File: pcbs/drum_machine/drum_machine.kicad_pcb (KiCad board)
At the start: 2 copper layers, 171 x 97 mm, 128 parts, among them Q1 NPN, Q10 NPN, Q11 NPN, Q12 NPN, Q13 NPN, Q14 NPN, Q15 NPN, Q16 NPN, Q2 NPN, Q3 NPN, Q4 NPN, Q5 NPN, Q6 NPN, Q7 NPN, Q8 NPN, Q9 NPN, SW1 SW_SPDT, SW10 SW_SPDT, SW11 SW_SPDT, SW12 SW_SPDT, SW13 SW_SPDT, SW14 SW_SPDT, SW15 SW_SPDT, SW16 SW_SPDT, SW17 SW_SPDT, SW18 SW_SPDT, SW19 SW_SPDT, SW2 SW_SPDT, SW20 SW_SPDT, SW21 SW_SPDT, SW22 SW_SPDT, SW23 SW_SPDT, SW24 SW_SPDT, SW25 SW_SPDT, SW26 SW_SPDT, SW27 SW_SPDT, SW28 SW_SPDT, SW29 SW_SPDT, SW3 SW_SPDT, SW30 SW_SPDT, SW31 SW_SPDT, SW32 SW_SPDT, SW33 SW_SPDT, SW34 SW_SPDT, SW35 SW_SPDT, SW36 SW_SPDT, SW37 SW_SPDT, SW38 SW_SPDT, SW39 SW_SPDT, SW4 SW_SPDT, SW40 SW_SPDT, SW41 SW_SPDT, SW42 SW_SPDT, SW43 SW_SPDT, SW44 SW_SPDT, SW45 SW_SPDT, SW46 SW_SPDT, SW47 SW_SPDT, SW48 SW_SPDT, SW49 SW_SPDT_CYMBAL, SW5 SW_SPDT, SW50 SW_SPDT_COUNTOFF, SW51 SW_SPDT_PLAYSTOP, SW52 SW_SPDT_LEDS, SW53 SW_SPDT_TIMESIG, SW54 SW_SPDT_RESERVED0, SW55 SW_SPDT_RESERVED1, SW56 SW_SPDT_RESERVED2, SW6 SW_SPDT, SW7 SW_SPDT, SW8 SW_SPDT, SW9 SW_SPDT, U1 CD4051B, U10 CD4051B, U11 CD4051B, U12 CD4051B, U2 Pico, U3 CD4051B, U4 CD4051B, U5 CD4051B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

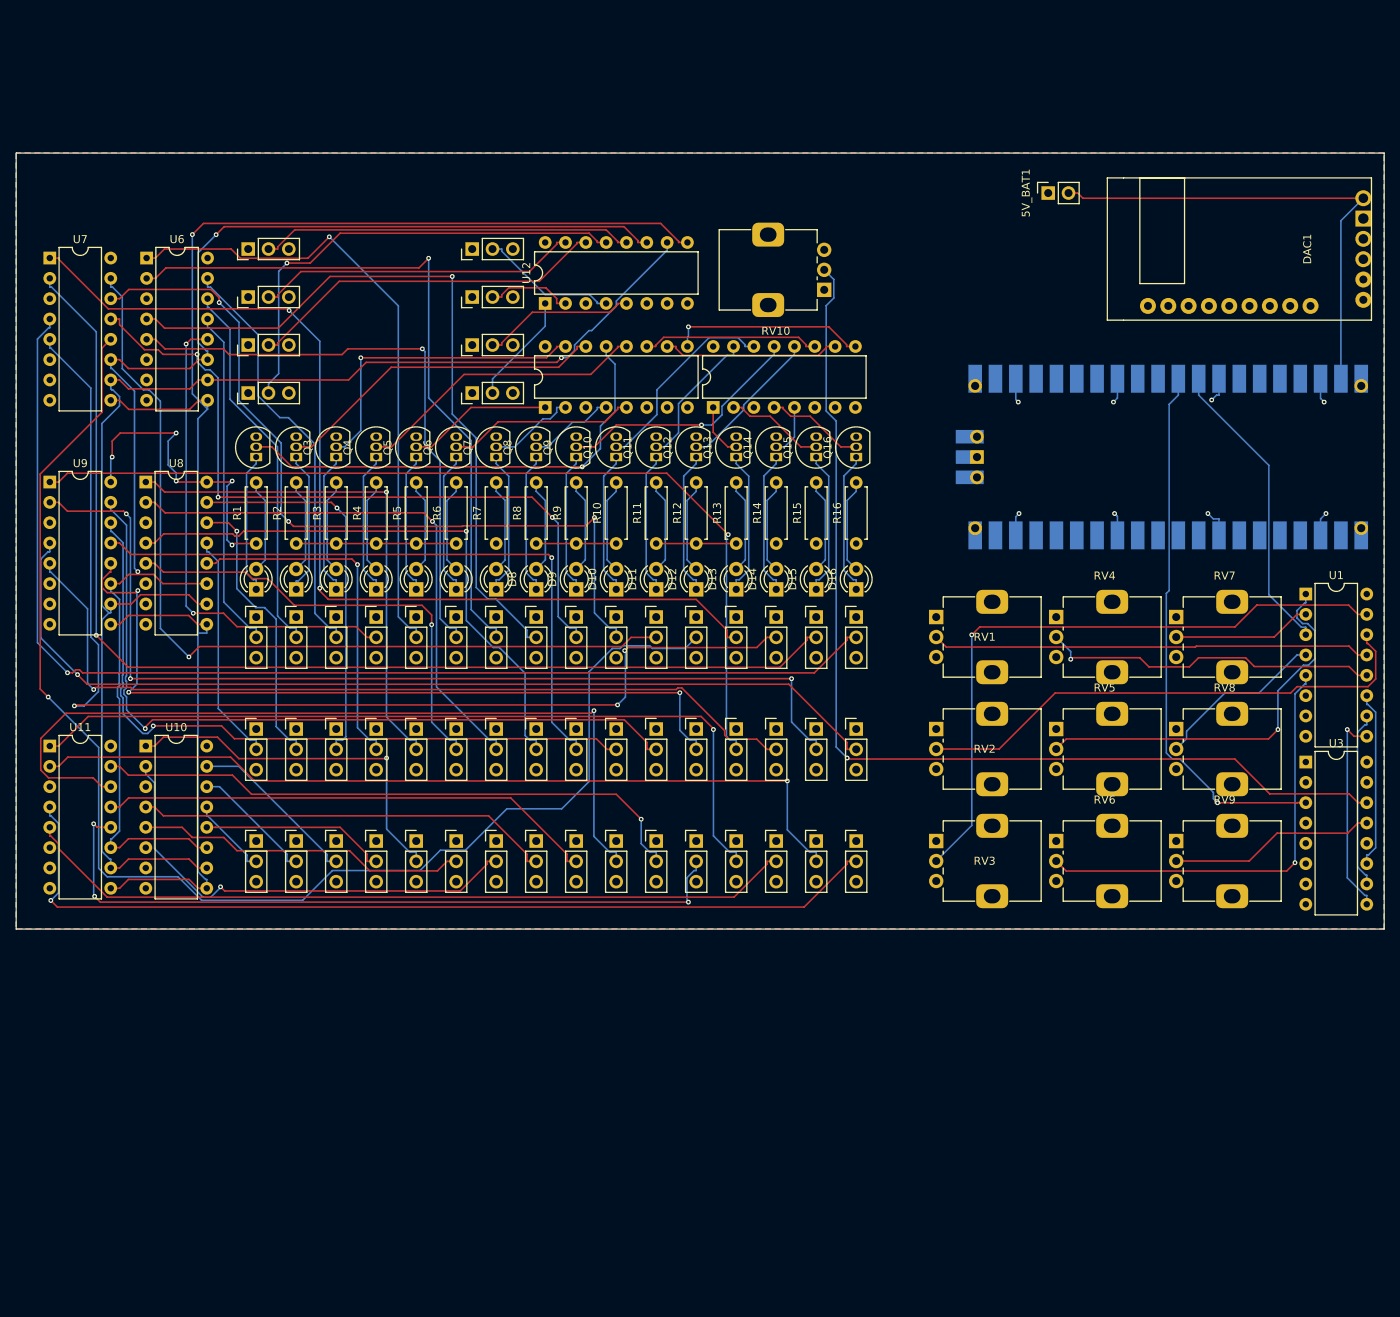
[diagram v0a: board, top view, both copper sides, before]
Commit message: Route drum machine
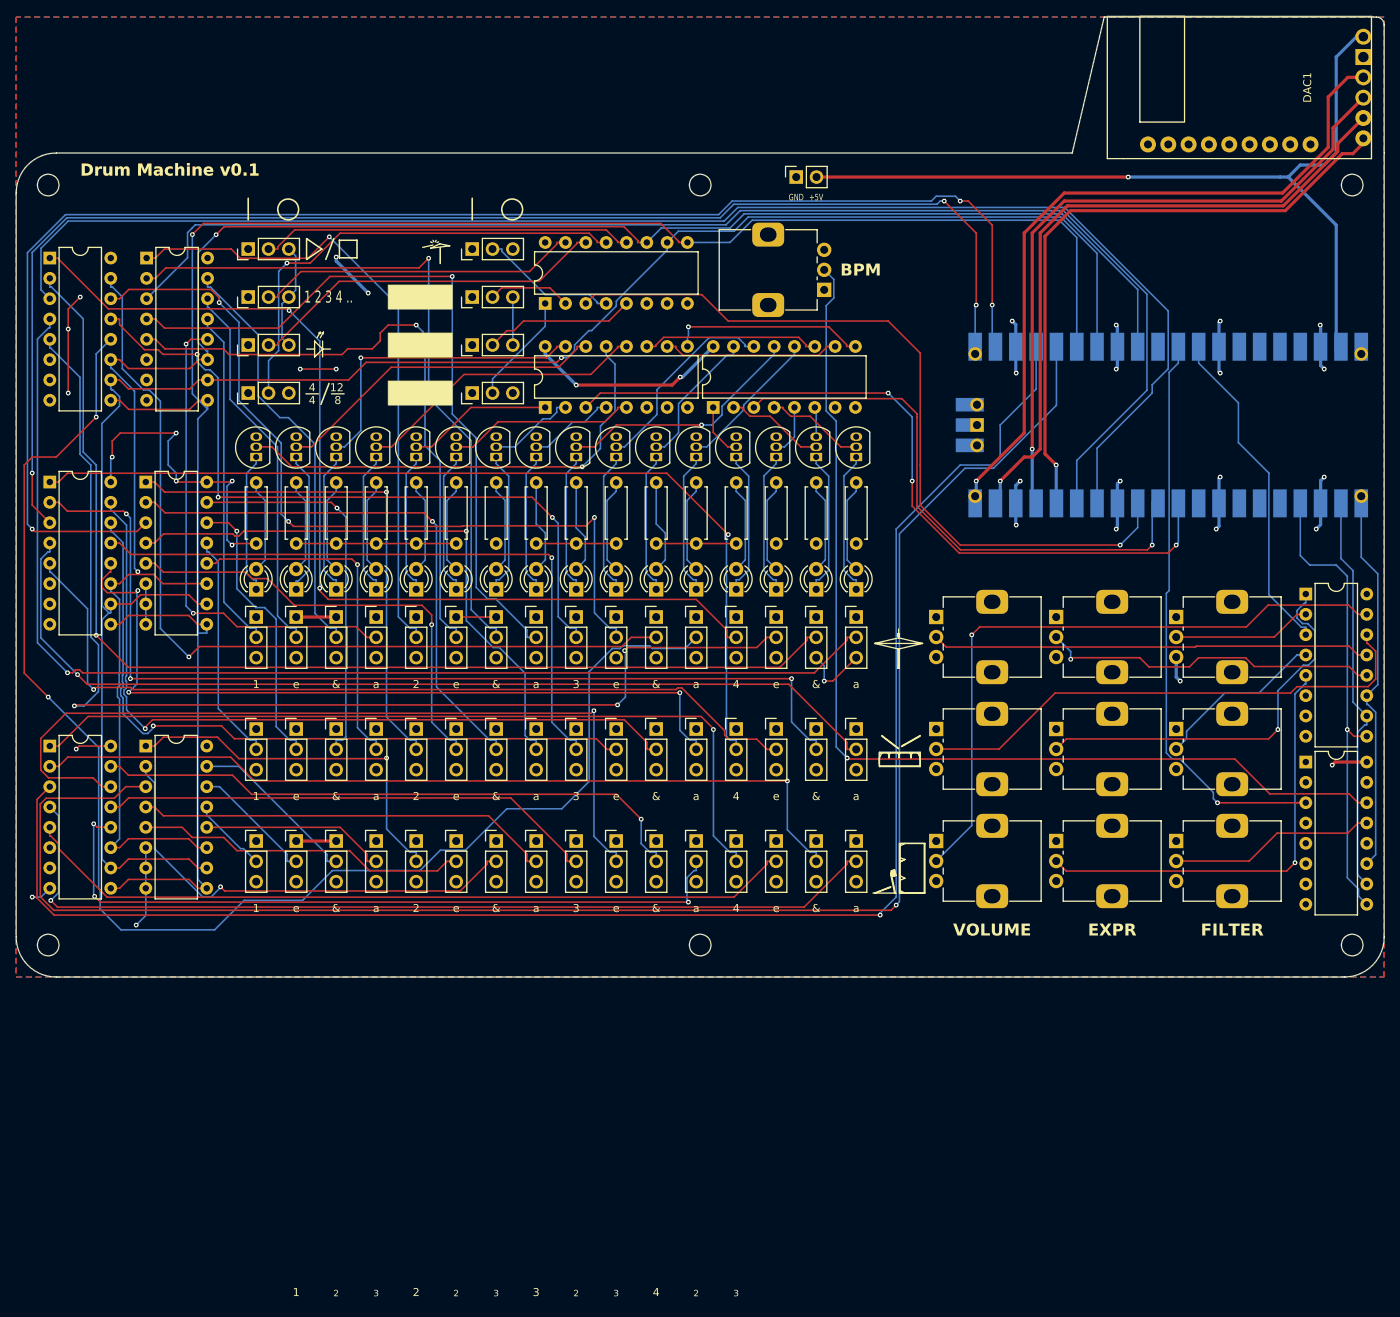
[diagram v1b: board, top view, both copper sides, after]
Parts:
- added H1: MountingHole, MountingHole:MountingHole_2.7mm_M2.5, F.Cu at (36.0, 52.0)
- added H2: MountingHole, MountingHole:MountingHole_2.7mm_M2.5, F.Cu at (36.0, 147.0)
- added H3: MountingHole, MountingHole:MountingHole_2.7mm_M2.5, F.Cu at (199.0, 52.0)
- added H4: MountingHole, MountingHole:MountingHole_2.7mm_M2.5, F.Cu at (199.0, 147.0)
- added H5: MountingHole, MountingHole:MountingHole_2.7mm_M2.5, F.Cu at (117.5, 52.0)
- added H6: MountingHole, MountingHole:MountingHole_2.7mm_M2.5, F.Cu at (117.5, 147.0)
- moved 5V_BAT1 31.6 mm to (129.5, 51.0)
- moved DAC1 20.2 mm to (201.4, 39.8)
- moved U2 4.00 mm to (176.0, 82.0)
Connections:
- U2 pad 1: unconnected-(U2-GPIO0-Pad1) -> /POT_ADDR0
- U2 pad 10: unconnected-(U2-GPIO7-Pad10) -> /LED_DRIVE0
- U2 pad 11: unconnected-(U2-GPIO8-Pad11) -> /LED_DRIVE1
- U2 pad 12: unconnected-(U2-GPIO9-Pad12) -> /SETTINGS_READ
- U2 pad 14: unconnected-(U2-GPIO10-Pad14) -> /HAT_READ_2_3
- U2 pad 15: unconnected-(U2-GPIO11-Pad15) -> /HAT_READ_1_2
- U2 pad 16: unconnected-(U2-GPIO12-Pad16) -> /SCK
- U2 pad 17: unconnected-(U2-GPIO13-Pad17) -> /DIN
- U2 pad 19: unconnected-(U2-GPIO14-Pad19) -> /BCK
- U2 pad 2: unconnected-(U2-GPIO1-Pad2) -> /POT_ADDR1
- U2 pad 20: unconnected-(U2-GPIO15-Pad20) -> /LRCK
- U2 pad 21: unconnected-(U2-GPIO16-Pad21) -> /SNARE_READ_2_3
- U2 pad 22: unconnected-(U2-GPIO17-Pad22) -> /SNARE_READ_1_2
- U2 pad 24: unconnected-(U2-GPIO18-Pad24) -> /KICK_READ_2_3
- U2 pad 25: unconnected-(U2-GPIO19-Pad25) -> /KICK_READ_1_2
- U2 pad 26: unconnected-(U2-GPIO20-Pad26) -> /PERC_ADDR2
- U2 pad 27: unconnected-(U2-GPIO21-Pad27) -> /PERC_ADDR1
- U2 pad 29: unconnected-(U2-GPIO22-Pad29) -> /PERC_ADDR0
- U2 pad 4: unconnected-(U2-GPIO2-Pad4) -> /POT_ADDR2
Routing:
- net /KICK_READ_1_2: track 0.00 -> 212.9 mm, vias 0 -> 1
- net /KICK_READ_2_3: track 0.00 -> 201.4 mm, vias 0 -> 1
- net /SNARE_READ_1_2: track 0.00 -> 190.9 mm, vias 0 -> 3
- net /HAT_READ_2_3: track 0.00 -> 182.0 mm
- net /SNARE_READ_2_3: track 0.00 -> 172.2 mm, vias 0 -> 3
- net /HAT_READ_1_2: track 0.00 -> 164.6 mm
- net /SETTINGS_READ: track 0.00 -> 98.4 mm, vias 0 -> 1
- net /LED_DRIVE0: track 0.00 -> 96.0 mm, vias 0 -> 3
- net GND: track 17.8 -> 109.2 mm, vias 8 -> 22
- net /LRCK: track 0.00 -> 90.2 mm, vias 0 -> 1
- net /DIN: track 0.00 -> 83.1 mm, vias 0 -> 1
- net /BCK: track 0.00 -> 82.7 mm, vias 0 -> 1
- net /SCK: track 0.00 -> 78.6 mm, vias 0 -> 1
- net /PERC_ADDR0: track 173.9 -> 248.7 mm
- net /LED_DRIVE1: track 0.00 -> 71.5 mm, vias 0 -> 1
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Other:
- board size 171 x 97 mm -> 171 x 120 mm
- board text added: "&"
- board text added: "+5V"
- board text added: "1"
- board text added: "1 2 3 4 .."
- board text added: "12"
- board text added: "2"
- board text added: "3"
- board text added: "4"
- board text added: "8"
- board text added: "BPM"
- board text added: "Drum Machine v0.1"
- board text added: "EXPR"
- board text added: "FILTER"
- board text added: "GND"
- board text added: "VOLUME"
- board text added: "a"
- board text added: "e"

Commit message: Connect LED addresses
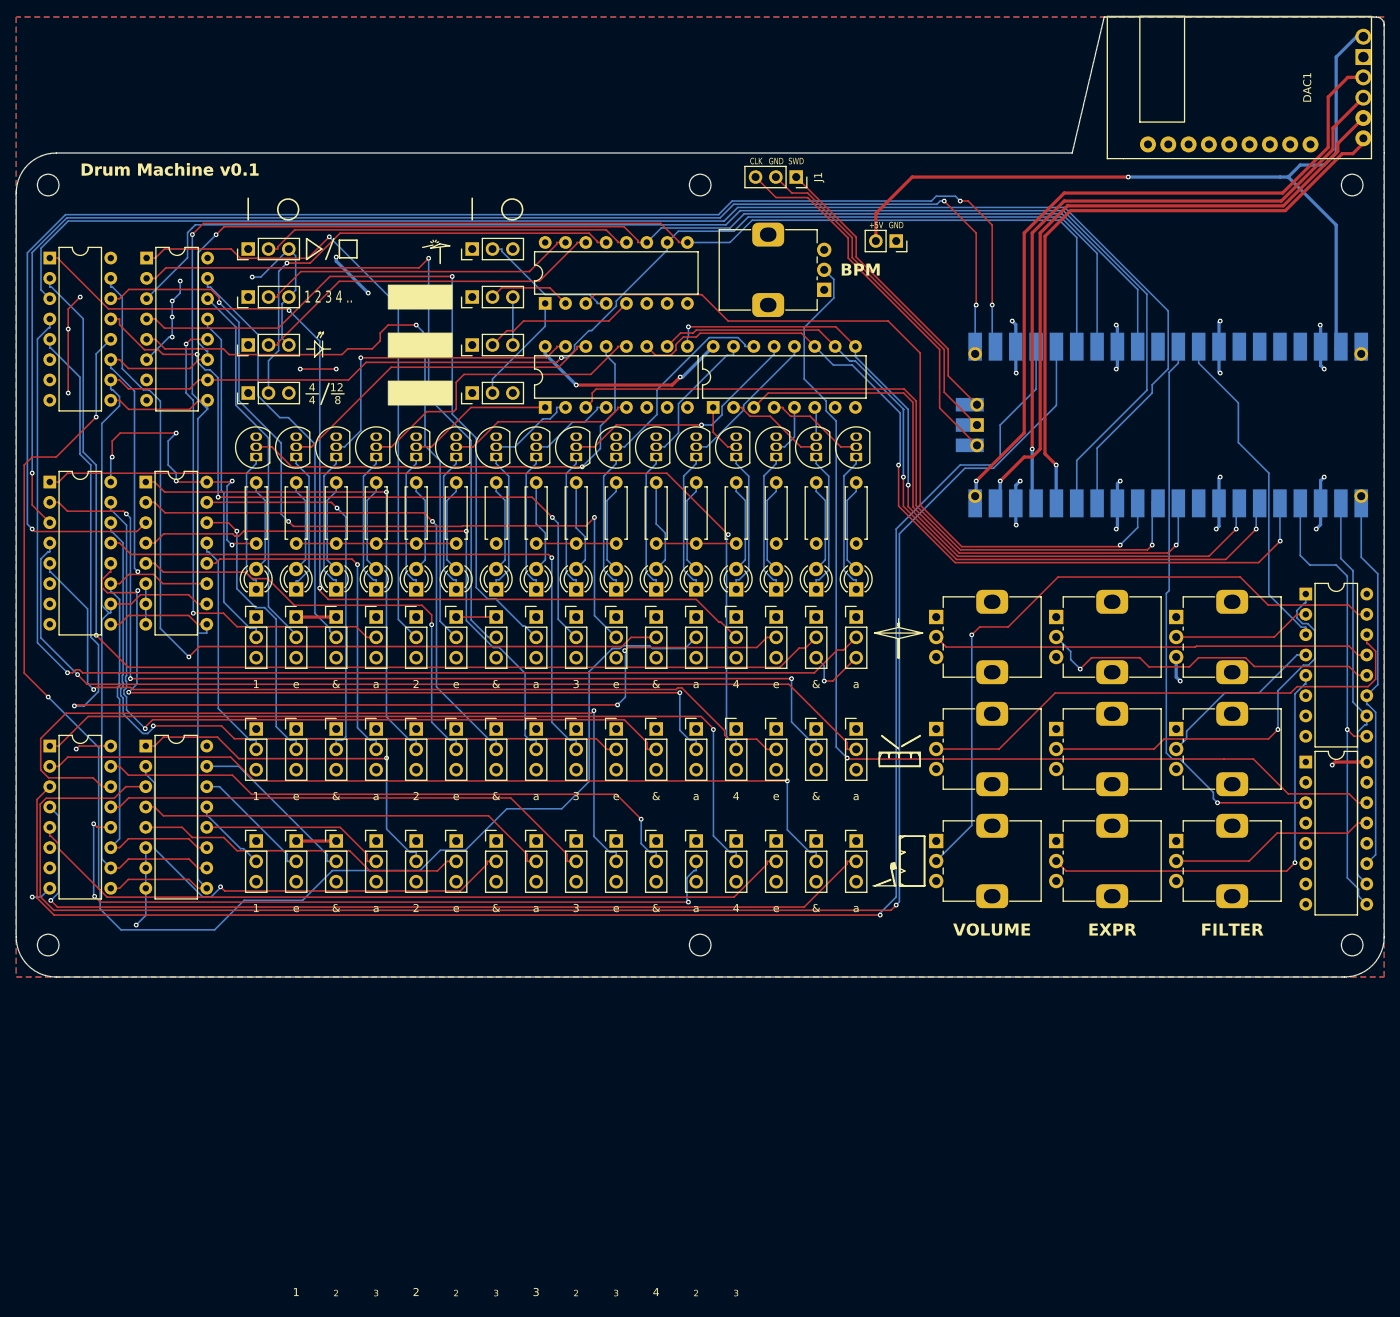
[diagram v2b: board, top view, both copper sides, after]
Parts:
- added J1: Conn_01x03, Connector_PinSocket_2.54mm:PinSocket_1x03_P2.54mm_Vertical, F.Cu at (129.5, 51.0)
- moved 5V_BAT1 14.8 mm to (142.0, 59.0), turned to -90 degrees
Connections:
- U2 pad 10: /LED_DRIVE0 -> /LED_DRIVE1
- U2 pad 11: /LED_DRIVE1 -> /LED_DRIVE0
- U2 pad 41: unconnected-(U2-SWCLK-Pad41) -> Net-(J1-Pin_3)
- U2 pad 42: unconnected-(U2-GND-Pad42) -> Net-(J1-Pin_2)
- U2 pad 43: unconnected-(U2-SWDIO-Pad43) -> Net-(J1-Pin_1)
- U2 pad 5: unconnected-(U2-GPIO3-Pad5) -> /LED_ADDR0
- U2 pad 6: unconnected-(U2-GPIO4-Pad6) -> /LED_ADDR1
- U2 pad 7: unconnected-(U2-GPIO5-Pad7) -> /LED_ADDR2
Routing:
- net /LED_ADDR0: track 22.2 -> 106.9 mm, vias 0 -> 2
- net /LED_ADDR1: track 22.1 -> 99.4 mm, vias 0 -> 2
- net /LED_ADDR2: track 24.5 -> 96.4 mm, vias 1 -> 3
- net Net-(J1-Pin_3): track 0.00 -> 47.3 mm
- net Net-(J1-Pin_2): track 0.00 -> 42.6 mm
- net Net-(J1-Pin_1): track 0.00 -> 37.8 mm
- net GND: track 109.2 -> 127.0 mm, vias 22 -> 27
- net /LED_DRIVE1: track 71.5 -> 76.1 mm
- net /POT2: track 81.5 -> 84.4 mm
- net /POT9: track 130.3 -> 132.5 mm
- net /LED_1A: track 36.6 -> 38.5 mm
- net +5V: track 108.4 -> 106.6 mm
- net /POT3: track 42.5 -> 43.5 mm
- net /LED_DRIVE0: track 96.0 -> 95.0 mm, vias 3 -> 1
- net /HAT_1E: track 47.5 -> 46.9 mm
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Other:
- board text added: "CLK"
- board text added: "SWD"
